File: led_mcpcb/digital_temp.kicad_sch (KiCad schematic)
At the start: 9 parts, among them U1 TMP112xxDRL

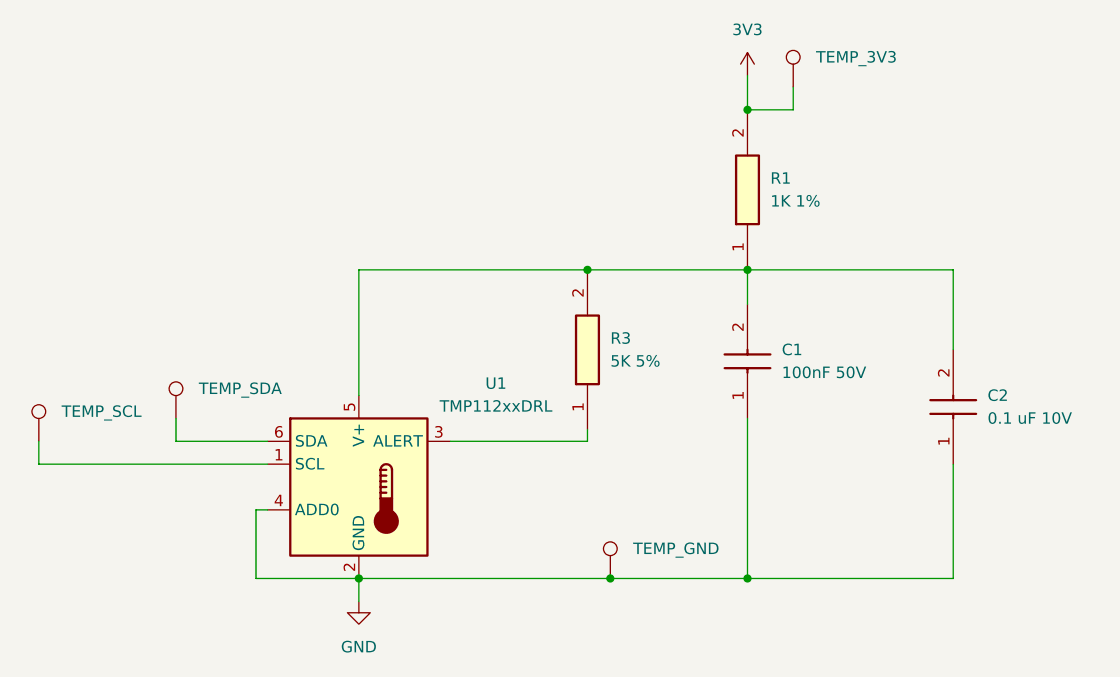
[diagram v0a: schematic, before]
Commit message: Finalize KiCad PCB sources for 5-piece test build
Commit the completed Open Vettam 15CCT KiCad source design files prepared for the initial five-piece production test run.

Included files are limited to the schematic hierarchy, PCB layouts, KiCad project files, and the LED MCPCB design-rules file. Generated BOM exports, fabrication output archives, freerouting/temp files, logs, backups, images, netlists, and Altium import artifacts are intentionally left unstaged.

Updated main controller board sources:

- open_vettam_15CCT.kicad_sch

- open_vettam_15CCT.kicad_pcb

- open_vettam_15CCT.kicad_pro

- 24v_Input.kicad_sch

- 24-5_buck.kicad_sch

- MCU.kicad_sch

- cc_driver.kicad_sch

Updated LED MCPCB sources:

- led_mcpcb/led_mcpcb.kicad_sch

- led_mcpcb/led_mcpcb.kicad_pcb

- led_mcpcb/led_mcpcb.kicad_pro

- led_mcpcb/led_mcpcb.kicad_dru

- led_mcpcb/CW-5000.kicad_sch

- led_mcpcb/WW-3000.kicad_sch

- led_mcpcb/digital_temp.kicad_sch
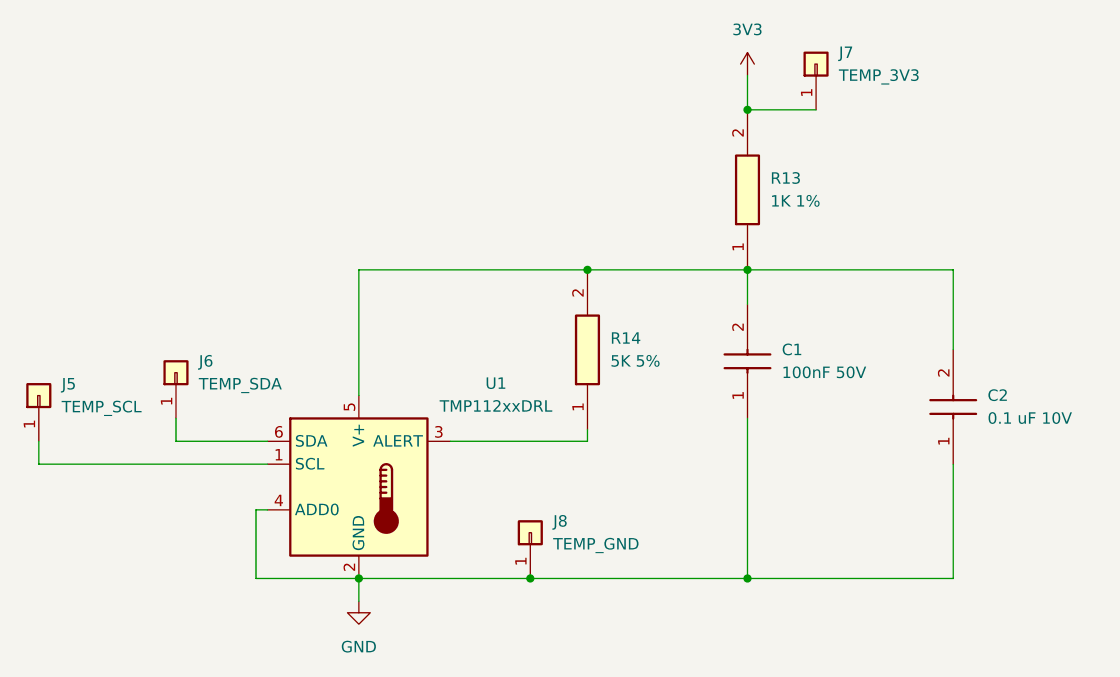
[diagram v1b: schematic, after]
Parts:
- removed TEMP_3V3, TEMP_GND: PAD, TestPoint:TestPoint_Pad_2.0x2.0mm, symbol Connector:TestPoint
- removed TEMP_SCL, TEMP_SDA: PAD, TestPoint:TestPoint_Pad_1.5x1.5mm, symbol Connector:TestPoint
- added J5: TEMP_SCL, Connector_Wire:SolderWirePad_1x01_SMD_1x2mm, symbol Connector_Generic:Conn_01x01
- added J6: TEMP_SDA, Connector_Wire:SolderWirePad_1x01_SMD_1x2mm, symbol Connector_Generic:Conn_01x01
- added J7: TEMP_3V3, Connector_Wire:SolderWirePad_1x01_SMD_1x2mm, symbol Connector_Generic:Conn_01x01
- added J8: TEMP_GND, Connector_Wire:SolderWirePad_1x01_SMD_1x2mm, symbol Connector_Generic:Conn_01x01
- U1: Manufacturer_Name (none) -> Texas Instruments; Manufacturer_Part_Number (none) -> TMP112AIDRLR; Mouser Part Number (none) -> 595-TMP112AIDRLR
- renumbered R1 to R13, R3 to R14
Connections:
- net 3V3: now also J7.1 (Pin_1)
- net GND: now also J8.1 (Pin_1)
- net at U1.1 (SCL): now also J5.1 (Pin_1)
- net at U1.6 (SDA): now also J6.1 (Pin_1)
